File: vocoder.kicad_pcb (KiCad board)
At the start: 2 copper layers, 47.2 x 35.6 mm, 36 parts, among them J1 AudioJack4, J2 Conn_01x02_Socket, J3 Conn_01x02_Pin, Q1 Q_NPN_BCE, Q2 Q_NPN_BCE, Q3 Q_NPN_BCE, Q4 Q_NPN_BCE, Q5 Q_NPN_BCE, SW1 SW_SPDT, SW2 SW_DIP_x05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

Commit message: changed sizes to JLCPCB acceptable sizes
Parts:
- R1, R10, R2, R3, R4, R5, R6, R7, R8, R9: footprint Resistor_SMD:R_0201_0603Metric -> Resistor_SMD:R_0603_1608Metric_Pad0.98x0.95mm_HandSolder
- moved C1 1.90 mm to (107.0, 80.0)
- moved R4 1.90 mm to (96.0, 70.3)
- moved R8 1.73 mm to (105.1, 81.9)
- moved R7 1.54 mm to (105.1, 78.6)
- moved R1 0.49 mm to (124.6, 82.5)
- moved R2 0.23 mm to (83.6, 82.5)
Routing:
- net GND: track 25.6 -> 22.7 mm
- net (no net): track 2.20 -> 0.00 mm, vias 2 -> 0
- net Net-(U3-FB): track 3.34 -> 4.97 mm
- net LED_LEFT: track 26.3 -> 27.2 mm, vias 1 -> 5
- net BATT_READ: track 3.29 -> 4.03 mm
- net Net-(R10-Pad1): track 1.18 -> 0.67 mm
- net 5V: track 47.0 -> 46.5 mm

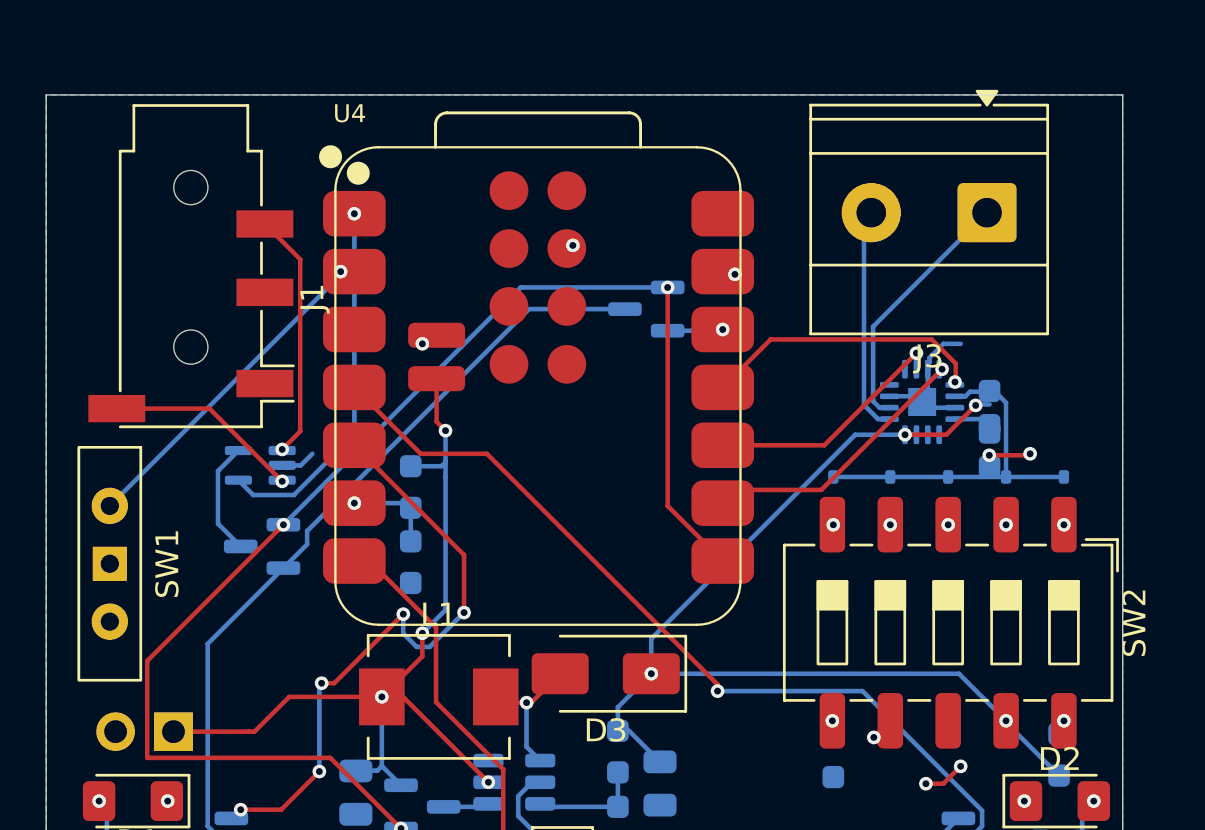
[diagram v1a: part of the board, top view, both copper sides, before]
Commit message: fixed component placement
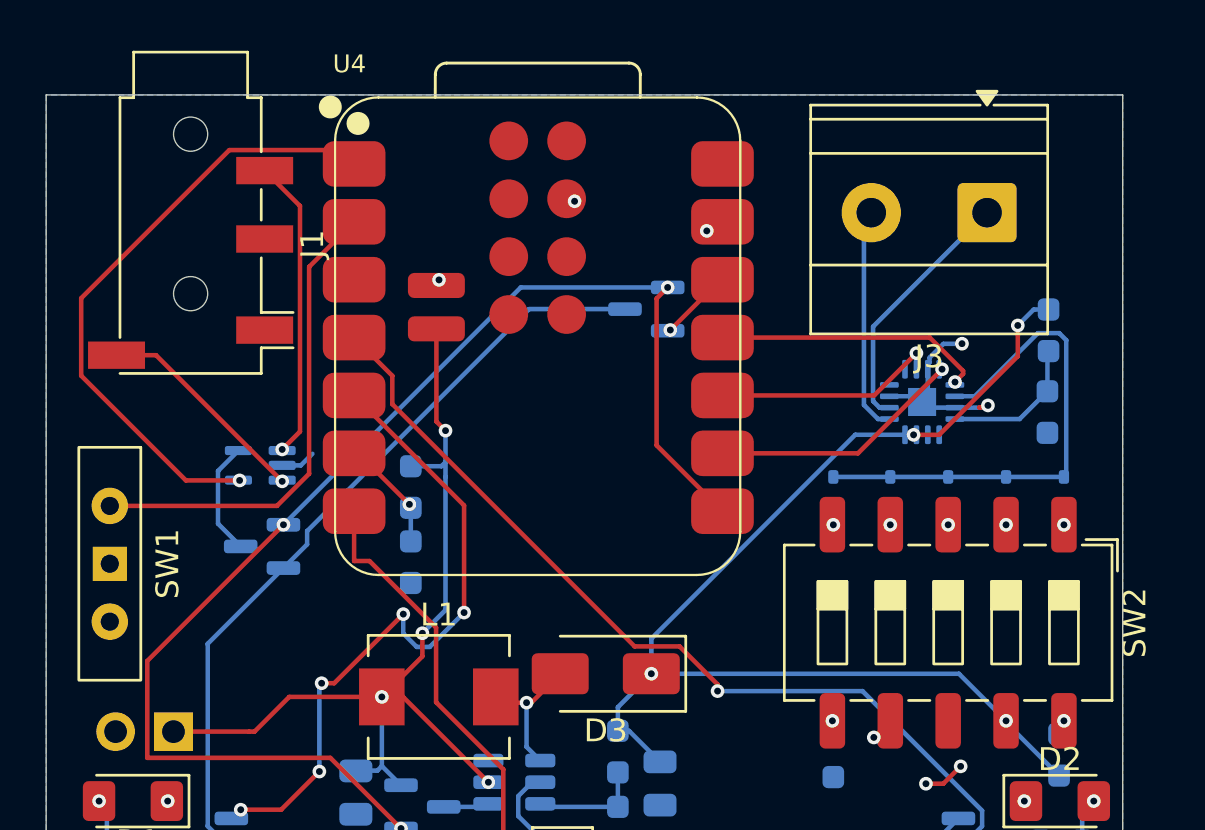
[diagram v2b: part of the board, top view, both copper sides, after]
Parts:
- moved R5 4.41 mm to (124.0, 60.1)
- moved R6 2.94 mm to (124.0, 63.7)
- moved J1 2.34 mm to (86.3, 56.3)
- moved U4 2.19 mm to (101.6, 60.4)
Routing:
- net MIC: track 16.1 -> 27.2 mm
- net SWITCH_INPUT: track 14.5 -> 21.2 mm, vias 1 -> 0
- net Net-(D4-K): track 15.9 -> 22.3 mm
- net 5V: track 46.5 -> 51.2 mm
- net Net-(U2-~{SD_MODE}): track 2.38 -> 6.35 mm
- net BATT+: track 37.7 -> 40.1 mm
- net Net-(U1-IN+): track 10.9 -> 13.2 mm
- net LED_LEFT: track 27.2 -> 29.4 mm
- net BUZZER: track 16.2 -> 18.4 mm
- net 3V3_SWITCH: track 59.7 -> 57.9 mm
- net LED_RIGHT: track 38.1 -> 39.7 mm
- net 3V3_PRE: track 2.44 -> 3.92 mm
- net Net-(U1-IN-): track 8.58 -> 9.56 mm
- net I2S_BCLK: track 12.1 -> 11.2 mm
- net I2S_LRCLK: track 10.9 -> 9.98 mm
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
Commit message: fixed grounding pad not attatched to ground plane
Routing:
- net GND: track 22.6 -> 24.7 mm, vias 10 -> 12
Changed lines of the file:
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@@
+	)
+	(segment
+		(start 124 64.65)
+		(end 124.05 64.6)
+		(width 0.2)
+		(layer "F.Cu")
+		(net 2)
 	)
 	(segment
@@
 	)
 	(segment
+		(start 124.05 64.6)
+		(end 126 64.6)
+		(width 0.2)
+		(layer "F.Cu")
+		(net 2)
+	)
+	(segment
 		(start 109.398 55.352)
 		(end 109 55.75)
@@
 	)
 	(via
+		(at 126 64.6)
+		(size 0.6)
+		(drill 0.3)
+		(layers "F.Cu" "B.Cu")
+		(net 2)
+	)
+	(via
 		(at 118.618 80.01)
 		(size 0.6)
@@
 	(via
 		(at 85.344 80.772)
+		(size 0.6)
+		(drill 0.3)
+		(layers "F.Cu" "B.Cu")
+		(net 2)
+	)
+	(via
+		(at 124 64.65)
 		(size 0.6)
 		(drill 0.3)
@@
 	)
 	(segment
+		(start 123.9625 64.6125)
+		(end 124 64.65)
+		(width 0.2)
+		(layer "B.Cu")
+		(net 2)
+	)
+	(segment
 		(start 118.7005 63.508)
 		(end 118.4505 63.258)
@@
 		(width 0.2)
 		(layer "B.Cu")
+		(net 2)
+	)
+	(segment
+		(start 123.95 64.6125)
+		(end 123.9625 64.6125)
+		(width 0.2)
+		(layer "B.Cu")

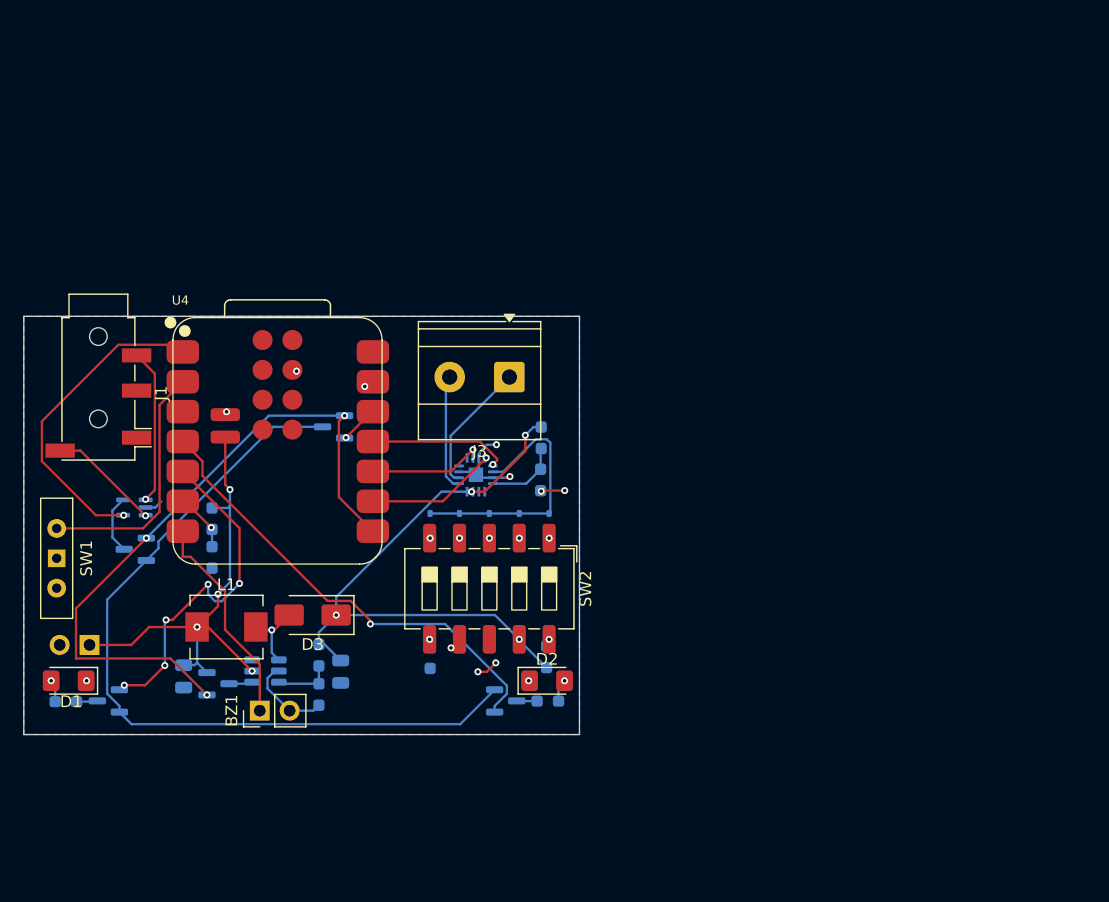
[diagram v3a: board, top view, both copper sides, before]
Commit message: complete redesign of board and circuit, smaller and more powerful
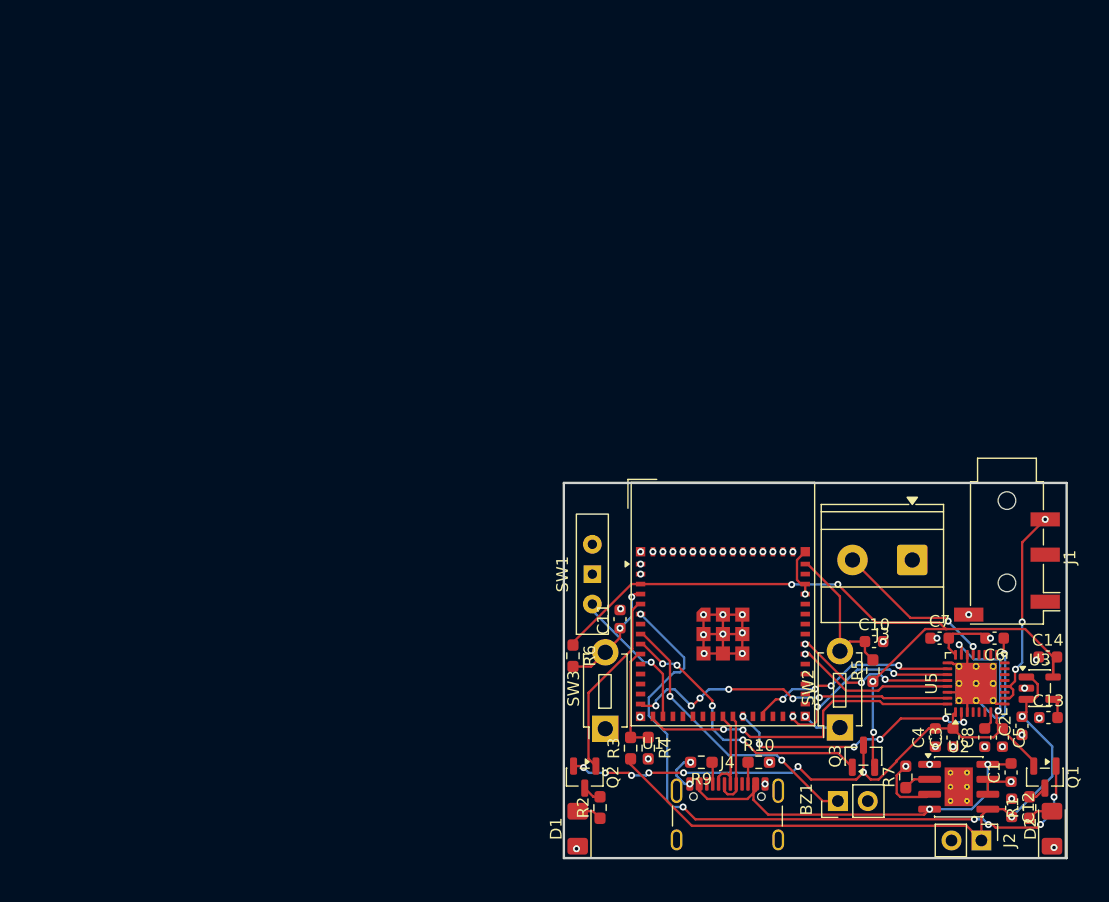
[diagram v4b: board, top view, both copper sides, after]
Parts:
- removed D3: SS34, Diode_SMD:D_SMA
- removed D4, D5, D6, D7, D8: 1N4148WS, Diode_SMD:D_SOD-323
- removed L1: 22u, Inductor_SMD:L_Neosid_SM-PIC0512H
- removed Q4, Q5: Q_NPN_BCE, Package_TO_SOT_SMD:SOT-23
- removed R8: 15k, Resistor_SMD:R_0603_1608Metric_Pad0.98x0.95mm_HandSolder
- removed U4: XIAO-ESP32-S3-SMD, Seeed Studio XIAO Series Library:XIAO-ESP32S3-SMD
- added C10: 0.1u, Capacitor_SMD:C_0603_1608Metric, F.Cu at (152.3, 77.4)
- added C11: 0.1u, Capacitor_SMD:C_0603_1608Metric, F.Cu at (130.7, 75.5)
- added C12: 1u, Capacitor_SMD:C_0603_1608Metric, F.Cu at (164.0, 91.6)
- added C13: 1u, Capacitor_SMD:C_0603_1608Metric, F.Cu at (167.1, 83.9)
- added C14: 1u, Capacitor_SMD:C_0603_1608Metric, F.Cu at (167.1, 78.8)
- added C3: 100n, Capacitor_SMD:C_0603_1608Metric, F.Cu at (159.0, 85.6)
- added C4: 10u, Capacitor_SMD:C_0603_1608Metric, F.Cu at (157.5, 85.6)
- added C5: 100n, Capacitor_SMD:C_0603_1608Metric, F.Cu at (163.2, 85.6)
- added C6: 100n, Capacitor_SMD:C_0603_1608Metric, F.Cu at (162.6, 77.2)
- added C7: 10u, Capacitor_SMD:C_0603_1608Metric, F.Cu at (157.9, 77.2)
- added C8: 10u, Capacitor_SMD:C_0603_1608Metric, F.Cu at (161.7, 85.6)
- added J4: USB_C_Receptacle_USB2.0_16P, Connector_USB:USB_C_Receptacle_GCT_USB4105-xx-A_16P_TopMnt_Horizontal, F.Cu at (139.8, 93.2)
- added SW3: SW_Push, Button_Switch_THT:SW_PUSH_1P1T_6x3.5mm_H5.0_APEM_MJTP1250, F.Cu at (129.4, 84.8)
- added U5: ADAU1761, Package_CSP:LFCSP-32-1EP_5x5mm_P0.5mm_EP3.5x3.5mm_ThermalVias, F.Cu at (161.0, 81.0)
- C1, C2: footprint Capacitor_SMD:C_0805_2012Metric -> Capacitor_SMD:C_0603_1608Metric; moved to F.Cu
- J2, Q1, Q2, Q3, R1, R2: moved to F.Cu
- R10, R9: value 100k -> 5.1k; moved to F.Cu
- R3: value 160 -> 10k; moved to F.Cu
- R4: value 160 -> 100k; moved to F.Cu
- R5: value 140 -> 10k; moved to F.Cu
- R6: value 1k -> 10k; moved to F.Cu
- R7: value 110k -> 1.2k; moved to F.Cu
- SW2: value SW_DIP_x05 -> SW_Push; footprint Button_Switch_SMD:SW_DIP_SPSTx05_Slide_6.7x14.26mm_W8.61mm_P2.54mm_LowProfile -> Button_Switch_THT:SW_PUSH_1P1T_6x3.5mm_H5.0_APEM_MJTP1250
- U1: value MAX4466EXK -> ESP32-S3-MINI-1; footprint MAX4466EXK:SOT65P210X110-5N -> RF_Module:ESP32-S2-MINI-1; moved to F.Cu
- U2: value MAX98357A -> TP4056-42-ESOP8; footprint Package_DFN_QFN:TQFN-16-1EP_3x3mm_P0.5mm_EP1.23x1.23mm -> Package_SO:SOIC-8-1EP_3.9x4.9mm_P1.27mm_EP2.41x3.3mm_ThermalVias; moved to F.Cu
- U3: value MT3608 -> TPS73633DBV; footprint Package_TO_SOT_SMD:SOT-23-6 -> Package_TO_SOT_SMD:SOT-23-5; moved to F.Cu
- moved J1 78.5 mm to (163.6, 70.2)
- moved J2 77.6 mm to (161.4, 94.3), turned to -90 degrees
- moved C2 71.4 mm to (164.9, 84.6), turned to 90 degrees
- moved U3 65.8 mm to (166.4, 81.4), turned to 0 degrees
- moved C1 57.6 mm to (163.9, 88.6), turned to 90 degrees
- moved Q3 53.0 mm to (151.4, 87.2), turned to 90 degrees
- moved R7 51.0 mm to (155.0, 89.0), turned to 90 degrees
- moved U1 50.7 mm to (139.4, 74.2), turned to 0 degrees
- moved BZ1 49.8 mm to (149.2, 91.0)
- moved U2 48.9 mm to (159.5, 89.8), turned to 0 degrees
- moved Q1 46.3 mm to (166.8, 89.0), turned to -90 degrees
- moved R2 46.3 mm to (129.0, 91.5), turned to 90 degrees
- moved SW1 45.6 mm to (128.3, 71.7), turned to 90 degrees
- moved D1 45.1 mm to (127.1, 93.3), turned to 90 degrees
- moved D2 44.7 mm to (167.4, 93.3), turned to 90 degrees
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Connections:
- C1 pad 1: 5V -> GND
- C1 pad 2: GND -> USB_5V
- C2 pad 1: BATT+ -> GND
- C2 pad 2: GND -> BATT+
- J1 pad R2: Net-(U1-IN+) -> Net-(U5-LINP)
- J1 pad S: Net-(U1-IN-) -> GND
- J3 pad 1: Net-(J3-Pin_1) -> GND
- R10 pad 1: Net-(R10-Pad1) -> Net-(J4-CC2)
- R10 pad 2: 5V -> GND
- R5 pad 1: 5V -> 3V3_PRE
- R5 pad 2: Net-(U2-~{SD_MODE}) -> EN
- R6 pad 1: Net-(U2-~{SD_MODE}) -> 3V3_PRE
- R6 pad 2: GND -> BOOT
- R7 pad 1: 5V -> Net-(U2-PROG)
- R7 pad 2: Net-(U3-FB) -> GND
- R9 pad 1: Net-(R9-Pad1) -> Net-(J4-CC1)
- SW2 pad 1: Net-(D4-A) -> GND
- SW2 pad 2: Net-(D5-A) -> EN
- U1 pad 1: Net-(U1-IN+) -> GND
- U1 pad 3: Net-(U1-IN-) -> 3V3_PRE
- U1 pad 4: MIC -> BOOT
- U1 pad 5: Net-(Q5-E) -> LED_LEFT
- U2 pad 1: I2S_DATA -> GND
- U2 pad 2: Net-(D4-K) -> Net-(U2-PROG)
- U2 pad 4: Net-(U2-~{SD_MODE}) -> USB_5V
- U2 pad 5: unconnected-(U2-NC-Pad5) -> BATT+
- U2 pad 6: unconnected-(U2-NC-Pad6) -> GND
- U2 pad 7: 5V -> GND
- U2 pad 8: 5V -> USB_5V
- U2 pad 9: Net-(J3-Pin_2) -> GND
- U3 pad 1: Net-(D3-A) -> BATT+
- U3 pad 3: Net-(U3-FB) -> BATT+
- U3 pad 5: BATT+ -> 3V3_PRE
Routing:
- net 3V3_PRE: track 3.92 -> 64.8 mm, vias 1 -> 4
- net 5V: track 51.2 -> 0.00 mm, vias 4 -> 0
- net GND: track 24.7 -> 61.6 mm, vias 12 -> 53
- net 3V3_SWITCH: track 57.9 -> 23.7 mm, vias 3 -> 4
- net USB_5V: track 0.00 -> 33.6 mm, vias 0 -> 2
- net SDA: track 0.00 -> 28.7 mm, vias 0 -> 6
- net SCL: track 0.00 -> 28.6 mm, vias 0 -> 2
- net MIC: track 27.2 -> 0.00 mm, vias 1 -> 0
- net I2S_MCLK: track 0.00 -> 22.5 mm, vias 0 -> 6
- net Net-(D4-K): track 22.3 -> 0.00 mm
- net LED_RIGHT: track 39.7 -> 57.9 mm, vias 1 -> 6
- net I2S_DATA_OUT: track 0.00 -> 18.0 mm, vias 0 -> 4
- net Net-(U5-LINP): track 0.00 -> 17.5 mm, vias 0 -> 3
- net I2S_DATA_IN: track 0.00 -> 16.4 mm, vias 0 -> 3
- net BATT+: track 40.1 -> 54.1 mm, vias 4 -> 2
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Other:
- board size 47.2 x 35.6 mm -> 42.8 x 31.9 mm

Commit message: fixed minor error
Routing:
- net GND: track 61.6 -> 37.4 mm, vias 53 -> 34
- net SDA: track 28.7 -> 27.9 mm

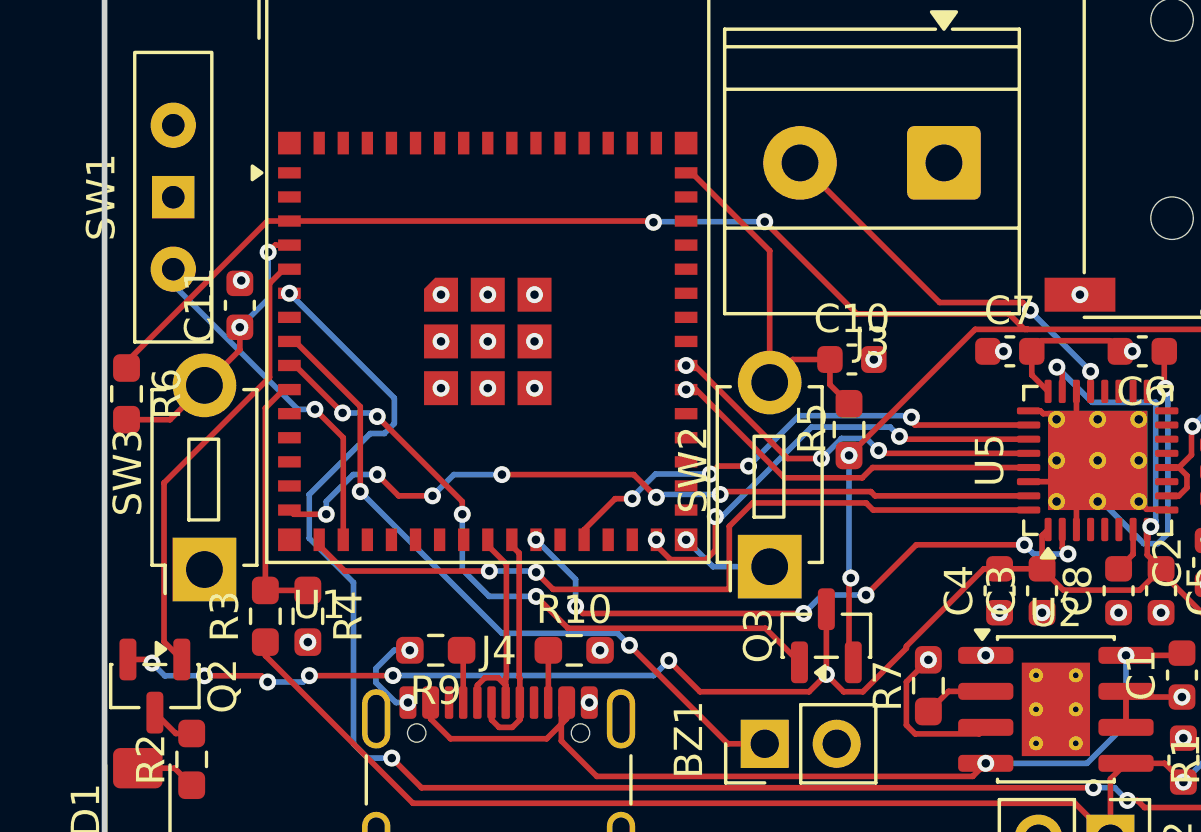
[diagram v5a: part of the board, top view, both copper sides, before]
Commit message: changed buttons to smaller SMT ones
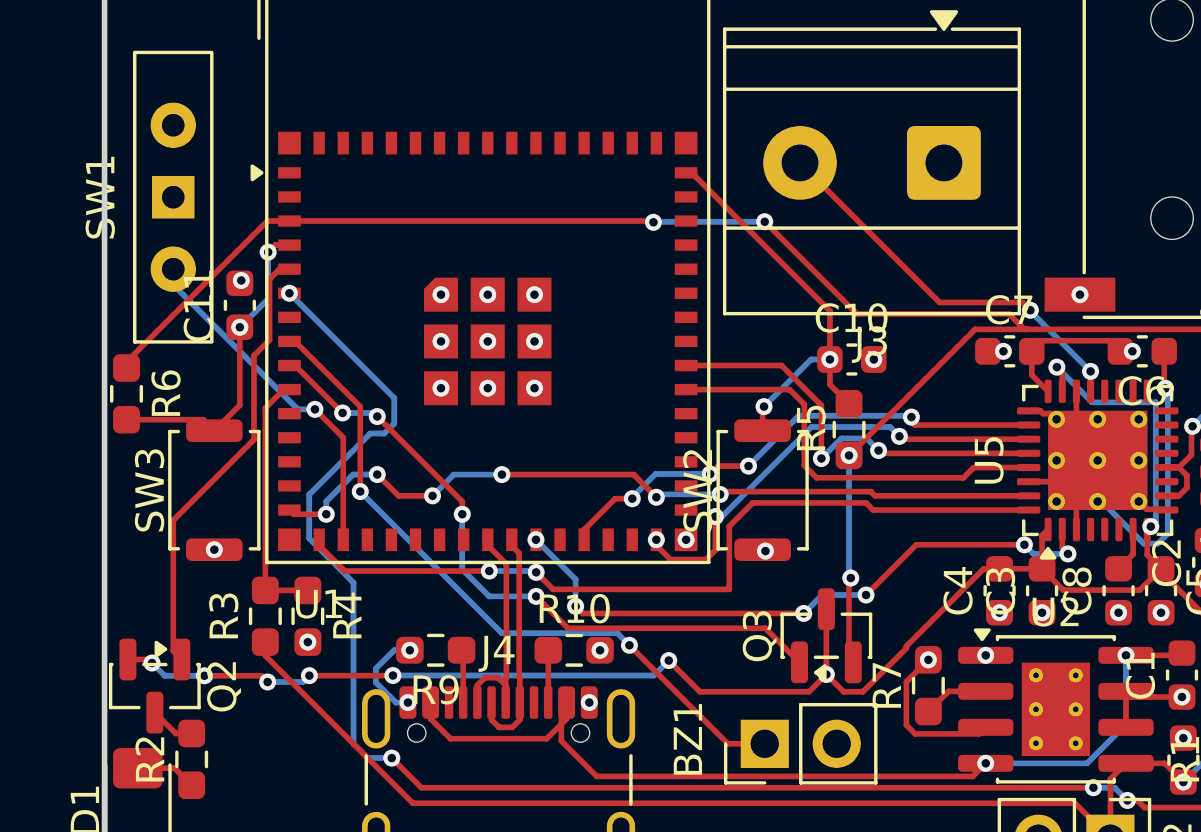
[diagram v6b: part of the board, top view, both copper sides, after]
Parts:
- SW2, SW3: footprint Button_Switch_THT:SW_PUSH_1P1T_6x3.5mm_H5.0_APEM_MJTP1250 -> Button_Switch_SMD:SW_Push_SPST_NO_Alps_SKRK
- moved SW3 2.82 mm to (129.8, 82.0)
- moved SW2 2.71 mm to (149.2, 82.0)
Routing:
- net GND: track 37.4 -> 34.2 mm, vias 34 -> 36
- net EN: track 13.0 -> 14.5 mm, vias 0 -> 2
- net BOOT: track 9.74 -> 11.2 mm
- net I2S_LRCLK: track 13.5 -> 14.8 mm, vias 1 -> 0
- net I2S_BCLK: track 14.0 -> 15.1 mm, vias 3 -> 2
